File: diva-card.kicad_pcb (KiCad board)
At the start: 2 copper layers, 85.4 x 53.7 mm, 95 parts, among them J1 Conn_02x05_Odd_Even, J2 USB_C_Receptacle_USB2.0, J3 Conn_02x21_Odd_Even, SW1 USER, SW2 BOOTSEL, SW3 RESET, U1 AP2112K-3.3, U2 ATECC608A-MAHDA, U3 W25Q128XXX, U4 RP2040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

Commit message: Production Design V1.0
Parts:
- added R16: 4.7k, Resistor_SMD:R_0402_1005Metric, F.Cu at (106.0, 84.5)
- added R5: 4.7k, Resistor_SMD:R_0402_1005Metric, F.Cu at (104.2, 83.1)
- moved FID1 23.3 mm to (65.4, 112.7)
- moved U2 1.17 mm to (106.0, 81.2)
- moved C16 0.11 mm to (97.3, 87.2)
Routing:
- net /I2C0_SDA: track 9.77 -> 11.2 mm
- net +3V3: track 57.7 -> 58.9 mm
- net /I2C0_SCL: track 11.4 -> 12.3 mm
- net /LED_DI: track 44.4 -> 43.5 mm
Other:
- board text added: "5V"
- board text added: "x x"
- board text removed: "+ -"
- board text removed: "USB"

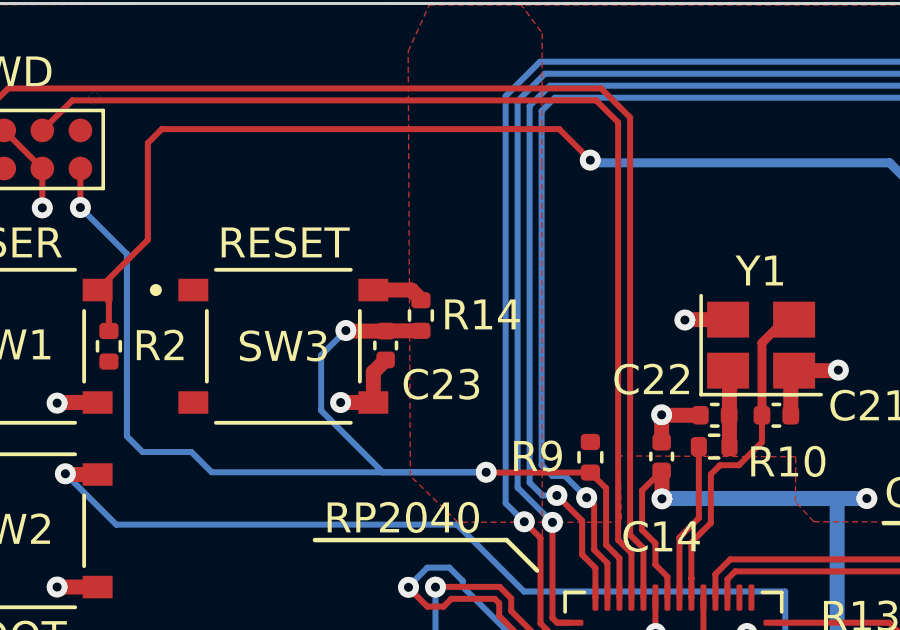
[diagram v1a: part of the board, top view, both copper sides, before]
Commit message: Fix issues found on production prototype
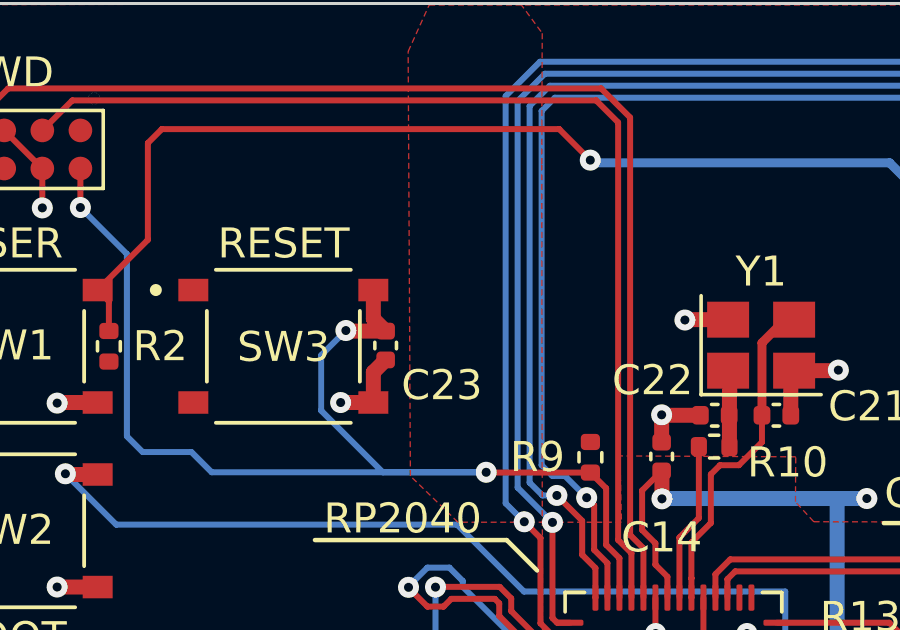
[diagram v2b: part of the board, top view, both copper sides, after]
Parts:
- removed R14: 10k, Resistor_SMD:R_0402_1005Metric
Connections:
- SW3 pad 1: Net-(R14-Pad2) -> /connectors/~{RESET}
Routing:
- net Net-(R14-Pad2): track 1.72 -> 0.00 mm
